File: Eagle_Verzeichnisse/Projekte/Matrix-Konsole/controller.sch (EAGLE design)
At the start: 20 parts, among them IC1 74HC165D

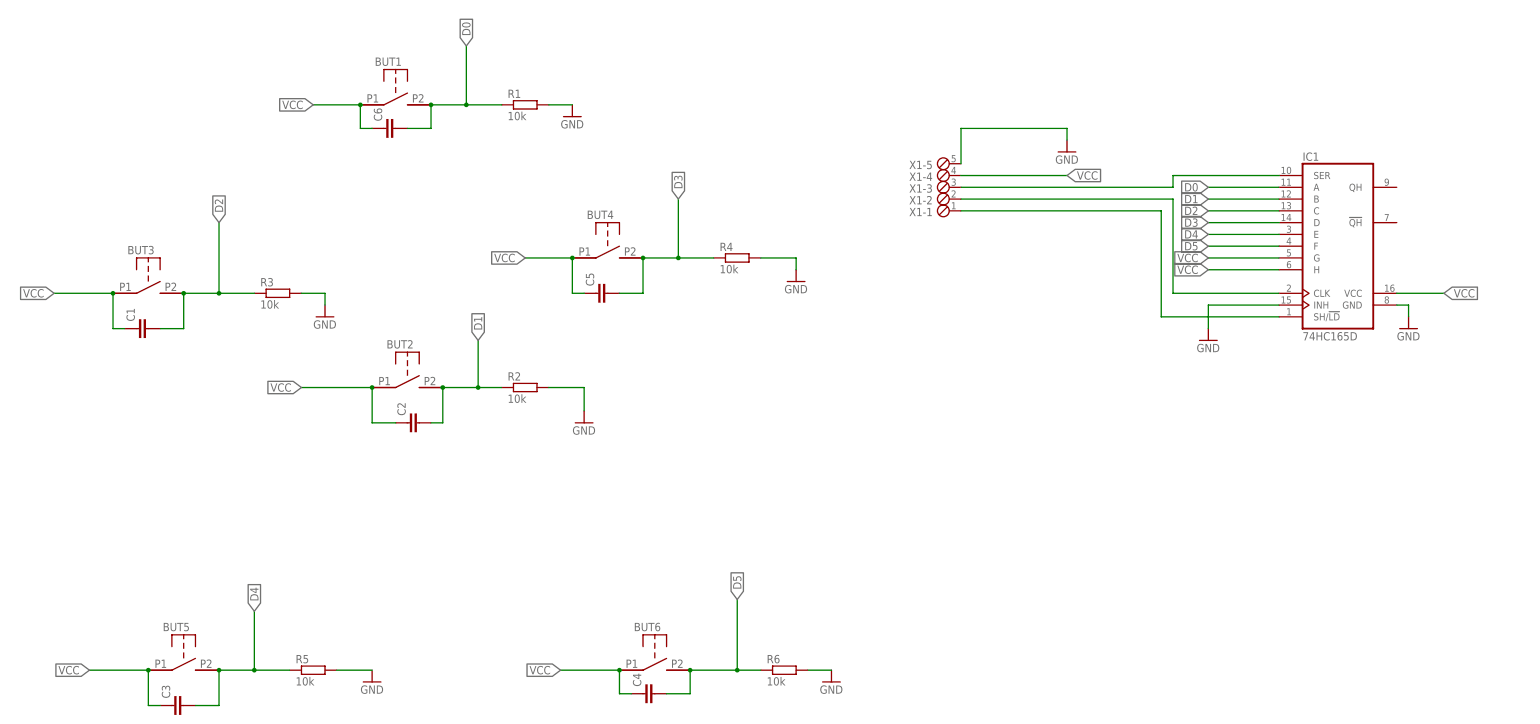
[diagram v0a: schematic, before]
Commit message: Added MAX7219, Added Potentiometer, Made curcuit diagram clearer, Changed Connectors
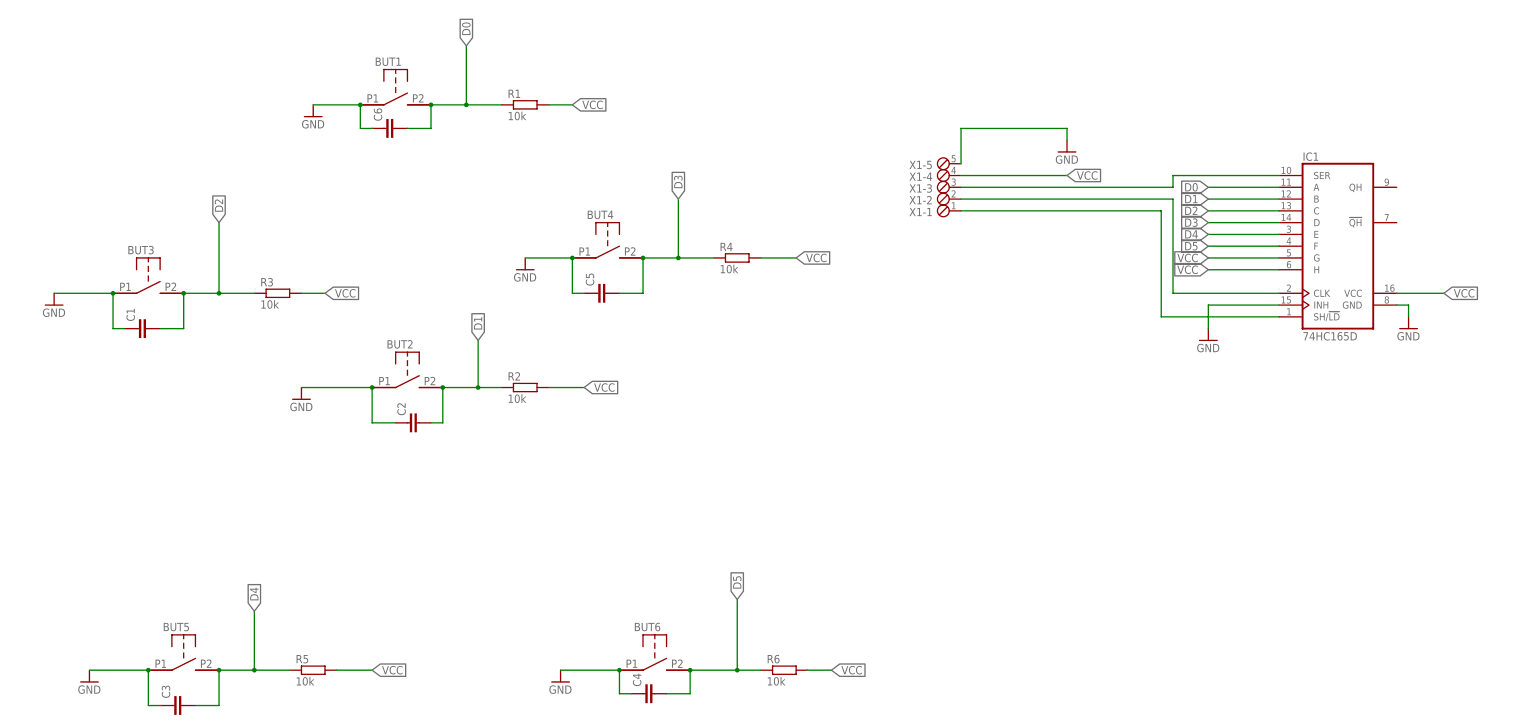
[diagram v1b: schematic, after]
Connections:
- new net N3: BUT4.P1, C5.1
- net GND: now also BUT1.P1, BUT2.P1, BUT3.P1, BUT5.P1, BUT6.P1, C1.1, C2.1, C3.1, C4.1, C6.1; no longer R1.2, R2.2, R3.2, R4.2, R5.2, R6.2
- net VCC: now also R1.2, R2.2, R3.2, R4.2, R5.2, R6.2; no longer BUT1.P1, BUT2.P1, BUT3.P1, BUT4.P1, BUT5.P1, BUT6.P1, C1.1, C2.1, C3.1, C4.1, C5.1, C6.1

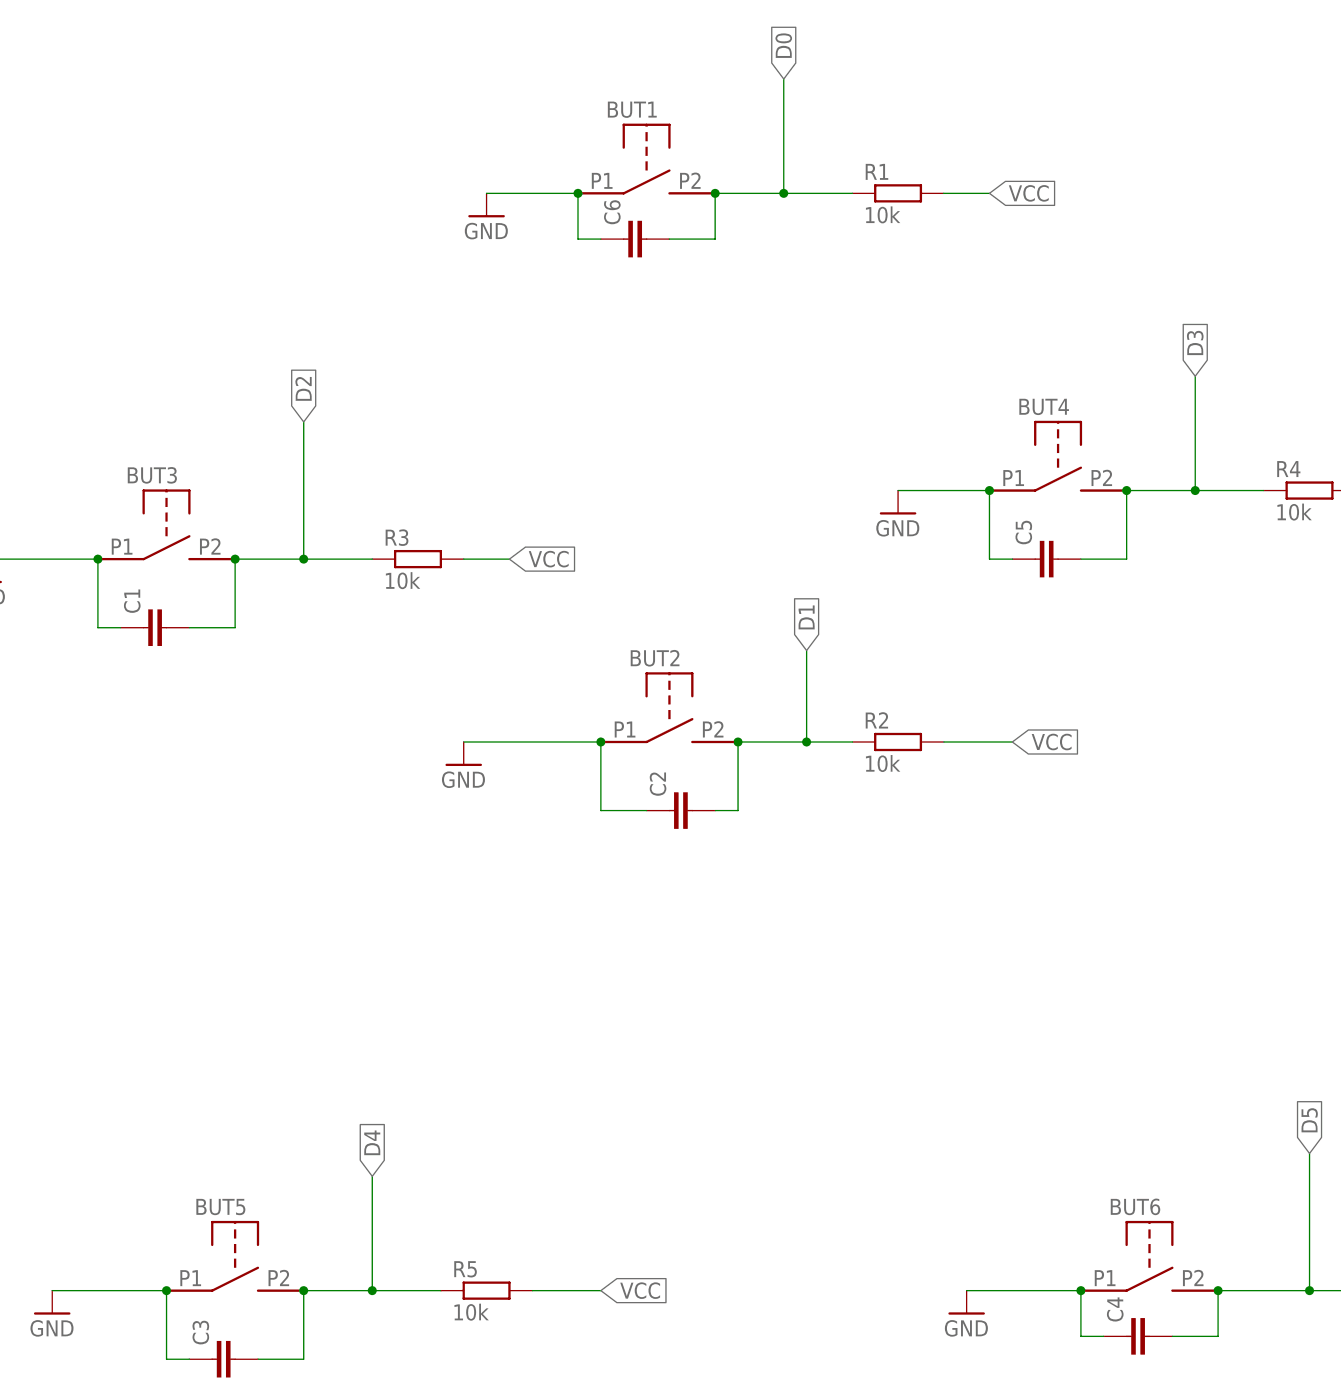
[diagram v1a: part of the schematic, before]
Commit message: Added Board to console, Added Pin header
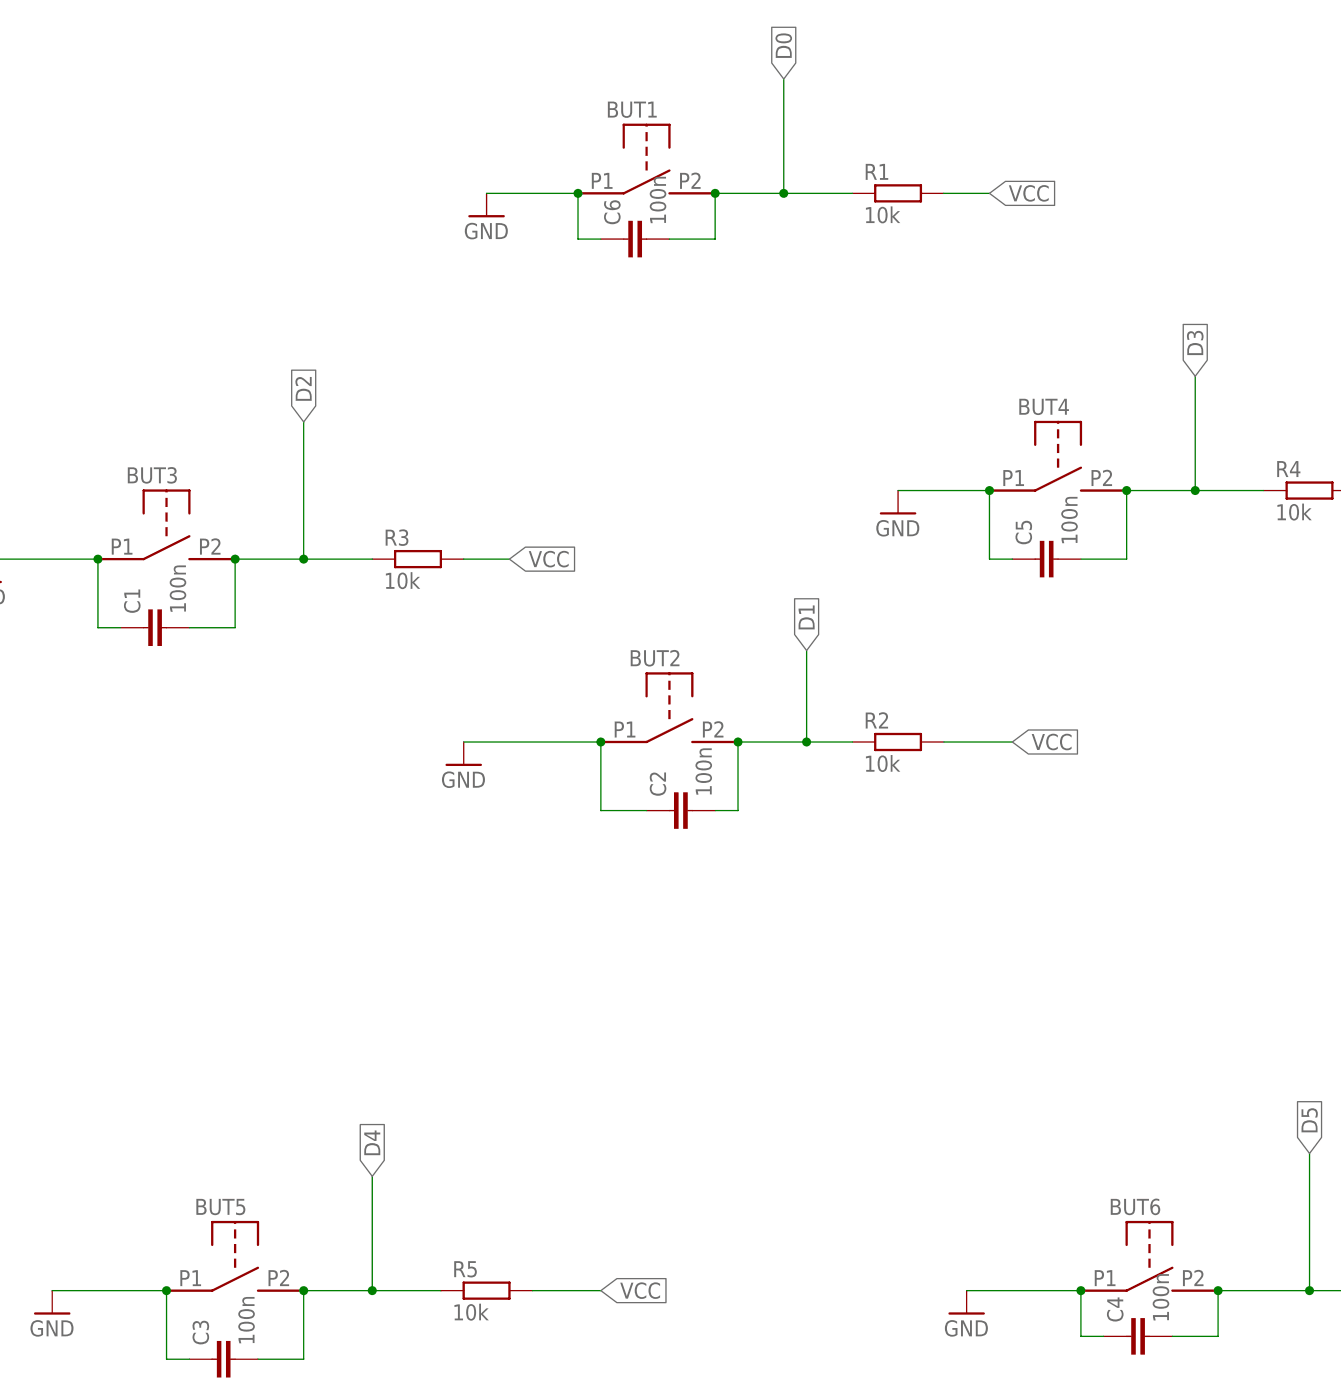
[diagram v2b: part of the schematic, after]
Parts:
- C1, C2, C3, C4, C5, C6: value (none) -> 100n
- R1, R2, R3, R4, R5, R6: device resistor:R-EU_0414/5V -> resistor:R-EU_M3516
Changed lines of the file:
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@@
 <setting verticaltext="up"/>
 </settings>
-<grid distance="0.1" unitdist="inch" unit="inch" style="lines" multiple="1" display="yes" altdistance="0.01" altunitdist="inch" altunit="inch"/>
+<grid distance="0.1" unitdist="inch" unit="inch" style="lines" multiple="1" display="no" altdistance="0.01" altunitdist="inch" altunit="inch"/>
 <layers>
 <layer number="1" name="Top" color="4" fill="1" visible="no" active="no"/>
@@
 <part name="BUT5" library="button" deviceset="BUTTON_DEV" device=""/>
 <part name="BUT6" library="button" deviceset="BUTTON_DEV" device=""/>
-<part name="R1" library="resistor" deviceset="R-EU_" device="0414/5V" value="10k"/>
-<part name="R2" library="resistor" deviceset="R-EU_" device="0414/5V" value="10k"/>
-<part name="R3" library="resistor" deviceset="R-EU_" device="0414/5V" value="10k"/>
-<part name="R4" library="resistor" deviceset="R-EU_" device="0414/5V" value="10k"/>
-<part name="R5" library="resistor" deviceset="R-EU_" device="0414/5V" value="10k"/>
-<part name="R6" library="resistor" deviceset="R-EU_" device="0414/5V" value="10k"/>
 <part name="IC1" library="74xx-eu" deviceset="74*165" device="D" technology="HC"/>
 <part name="GND1" library="supply1" deviceset="GND" device=""/>
@@
 <part name="X1" library="con-phoenix-254" deviceset="MPT5" device=""/>
 <part name="GND9" library="supply1" deviceset="GND" device=""/>
-<part name="C1" library="eagle-ltspice" deviceset="C" device=""/>
-<part name="C2" library="eagle-ltspice" deviceset="C" device=""/>
-<part name="C3" library="eagle-ltspice" deviceset="C" device=""/>
-<part name="C4" library="eagle-ltspice" deviceset="C" device=""/>
-<part name="C5" library="eagle-ltspice" deviceset="C" device=""/>
-<part name="C6" library="eagle-ltspice" deviceset="C" device=""/>
+<part name="C1" library="eagle-ltspice" deviceset="C" device="" value="100n"/>
+<part name="C2" library="eagle-ltspice" deviceset="C" device="" value="100n"/>
+<part name="C3" library="eagle-ltspice" deviceset="C" device="" value="100n"/>
+<part name="C4" library="eagle-ltspice" deviceset="C" device="" value="100n"/>
+<part name="C5" library="eagle-ltspice" deviceset="C" device="" value="100n"/>
+<part name="C6" library="eagle-ltspice" deviceset="C" device="" value="100n"/>
 <part name="GND2" library="supply1" deviceset="GND" device=""/>
 <part name="GND3" library="supply1" deviceset="GND" device=""/>
@@
 <part name="GND6" library="supply1" deviceset="GND" device=""/>
 <part name="GND7" library="supply1" deviceset="GND" device=""/>
+<part name="R1" library="resistor" deviceset="R-EU_" device="M3516" value="10k"/>
+<part name="R2" library="resistor" deviceset="R-EU_" device="M3516" value="10k"/>
+<part name="R3" library="resistor" deviceset="R-EU_" device="M3516" value="10k"/>
+<part name="R4" library="resistor" deviceset="R-EU_" device="M3516" value="10k"/>
+<part name="R5" library="resistor" deviceset="R-EU_" device="M3516" value="10k"/>
+<part name="R6" library="resistor" deviceset="R-EU_" device="M3516" value="10k"/>
 </parts>
 <sheets>
@@
 <instance part="BUT5" gate="G$1" x="-226.06" y="-48.26"/>
 <instance part="BUT6" gate="G$1" x="-124.46" y="-48.26"/>
-<instance part="R1" gate="G$1" x="-152.4" y="73.66"/>
-<instance part="R2" gate="G$1" x="-152.4" y="12.7"/>
-<instance part="R3" gate="G$1" x="-205.74" y="33.02"/>
-<instance part="R4" gate="G$1" x="-106.68" y="40.64"/>
-<instance part="R5" gate="G$1" x="-198.12" y="-48.26"/>
-<instance part="R6" gate="G$1" x="-96.52" y="-48.26"/>
 <instance part="IC1" gate="A" x="22.86" y="43.18"/>
 <instance part="GND1" gate="1" x="38.1" y="25.4"/>
@@
 <instance part="GND6" gate="1" x="-144.78" y="-50.8"/>
 <instance part="GND7" gate="1" x="-200.66" y="10.16"/>
+<instance part="R1" gate="G$1" x="-152.4" y="73.66"/>
+<instance part="R2" gate="G$1" x="-152.4" y="12.7"/>
+<instance part="R3" gate="G$1" x="-205.74" y="33.02"/>
+<instance part="R4" gate="G$1" x="-106.68" y="40.64"/>
+<instance part="R5" gate="G$1" x="-198.12" y="-48.26"/>
+<instance part="R6" gate="G$1" x="-96.52" y="-48.26"/>
 </instances>
 <busses>
@@
 </segment>
 <segment>
-<pinref part="R1" gate="G$1" pin="2"/>
 <wire x1="-147.32" y1="73.66" x2="-142.24" y2="73.66" width="0.1524" layer="91"/>
 <label x="-142.24" y="73.66" size="1.778" layer="95" xref="yes"/>
-</segment>
-<segment>
-<pinref part="R4" gate="G$1" pin="2"/>
+<pinref part="R1" gate="G$1" pin="2"/>
+</segment>
+<segment>
 <wire x1="-101.6" y1="40.64" x2="-93.98" y2="40.64" width="0.1524" layer="91"/>
 <label x="-93.98" y="40.64" size="1.778" layer="95" xref="yes"/>
-</segment>
-<segment>
-<pinref part="R2" gate="G$1" pin="2"/>
+<pinref part="R4" gate="G$1" pin="2"/>
+</segment>
+<segment>
 <wire x1="-147.32" y1="12.7" x2="-139.7" y2="12.7" width="0.1524" layer="91"/>
 <label x="-139.7" y="12.7" size="1.778" layer="95" xref="yes"/>
-</segment>
-<segment>
-<pinref part="R3" gate="G$1" pin="2"/>
+<pinref part="R2" gate="G$1" pin="2"/>
+</segment>
+<segment>
 <wire x1="-200.66" y1="33.02" x2="-195.58" y2="33.02" width="0.1524" layer="91"/>
 <label x="-195.58" y="33.02" size="1.778" layer="95" xref="yes"/>
-</segment>
-<segment>
-<pinref part="R5" gate="G$1" pin="2"/>
+<pinref part="R3" gate="G$1" pin="2"/>
+</segment>
+<segment>
 <wire x1="-193.04" y1="-48.26" x2="-185.42" y2="-48.26" width="0.1524" layer="91"/>
 <label x="-185.42" y="-48.26" size="1.778" layer="95" xref="yes"/>
-</segment>
-<segment>
-<pinref part="R6" gate="G$1" pin="2"/>
+<pinref part="R5" gate="G$1" pin="2"/>
+</segment>
+<segment>
 <wire x1="-91.44" y1="-48.26" x2="-86.36" y2="-48.26" width="0.1524" layer="91"/>
 <label x="-86.36" y="-48.26" size="1.778" layer="95" xref="yes"/>
+<pinref part="R6" gate="G$1" pin="2"/>
 </segment>
 </net>
@@
 <segment>
 <pinref part="BUT1" gate="G$1" pin="P2"/>
-<pinref part="R1" gate="G$1" pin="1"/>
 <wire x1="-172.72" y1="73.66" x2="-165.1" y2="73.66" width="0.1524" layer="91"/>
 <junction x="-165.1" y="73.66"/>
@@
 <wire x1="-172.72" y1="68.58" x2="-172.72" y2="73.66" width="0.1524" layer="91"/>
 <junction x="-172.72" y="73.66"/>
+<pinref part="R1" gate="G$1" pin="1"/>
 </segment>
 </net>
@@
 <segment>
 <pinref part="BUT2" gate="G$1" pin="P2"/>
-<pinref part="R2" gate="G$1" pin="1"/>
 <wire x1="-170.18" y1="12.7" x2="-162.56" y2="12.7" width="0.1524" layer="91"/>
 <junction x="-162.56" y="12.7"/>
@@
 <wire x1="-170.18" y1="5.08" x2="-170.18" y2="12.7" width="0.1524" layer="91"/>
 <junction x="-170.18" y="12.7"/>
+<pinref part="R2" gate="G$1" pin="1"/>
 </segment>
 </net>
@@
 <segment>
 <pinref part="BUT3" gate="G$1" pin="P2"/>
-<pinref part="R3" gate="G$1" pin="1"/>
 <wire x1="-226.06" y1="33.02" x2="-218.44" y2="33.02" width="0.1524" layer="91"/>
 <junction x="-218.44" y="33.02"/>
@@
 <wire x1="-226.06" y1="25.4" x2="-226.06" y2="33.02" width="0.1524" layer="91"/>
 <junction x="-226.06" y="33.02"/>
+<pinref part="R3" gate="G$1" pin="1"/>
 </segment>
 </net>
@@
 <segment>
 <pinref part="BUT4" gate="G$1" pin="P2"/>
-<pinref part="R4" gate="G$1" pin="1"/>
 <wire x1="-127" y1="40.64" x2="-119.38" y2="40.64" width="0.1524" layer="91"/>
 <junction x="-119.38" y="40.64"/>
@@
 <wire x1="-127" y1="33.02" x2="-127" y2="40.64" width="0.1524" layer="91"/>
 <junction x="-127" y="40.64"/>
+<pinref part="R4" gate="G$1" pin="1"/>
 </segment>
 </net>
@@
 <segment>
 <pinref part="BUT5" gate="G$1" pin="P2"/>
-<pinref part="R5" gate="G$1" pin="1"/>
 <wire x1="-218.44" y1="-48.26" x2="-210.82" y2="-48.26" width="0.1524" layer="91"/>
 <junction x="-210.82" y="-48.26"/>
@@
 <wire x1="-218.44" y1="-55.88" x2="-218.44" y2="-48.26" width="0.1524" layer="91"/>
 <junction x="-218.44" y="-48.26"/>
+<pinref part="R5" gate="G$1" pin="1"/>
 </segment>
 </net>
@@
 <segment>
 <pinref part="BUT6" gate="G$1" pin="P2"/>
-<pinref part="R6" gate="G$1" pin="1"/>
 <wire x1="-116.84" y1="-48.26" x2="-106.68" y2="-48.26" width="0.1524" layer="91"/>
 <junction x="-106.68" y="-48.26"/>
@@
 <wire x1="-116.84" y1="-53.34" x2="-116.84" y2="-48.26" width="0.1524" layer="91"/>
 <junction x="-116.84" y="-48.26"/>
-</segment>
-</net>
+<pinref part="R6" gate="G$1" pin="1"/>
+</segment>
+</net>
